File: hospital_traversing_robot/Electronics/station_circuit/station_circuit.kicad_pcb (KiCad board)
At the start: 2 copper layers, 17 parts, among them J1 Barrel_Jack_MountingPin, SW1 SW_Nidec_CAS-120A1, U1 Pico, U2 NRF24L01_Breakout, U3 LM338T

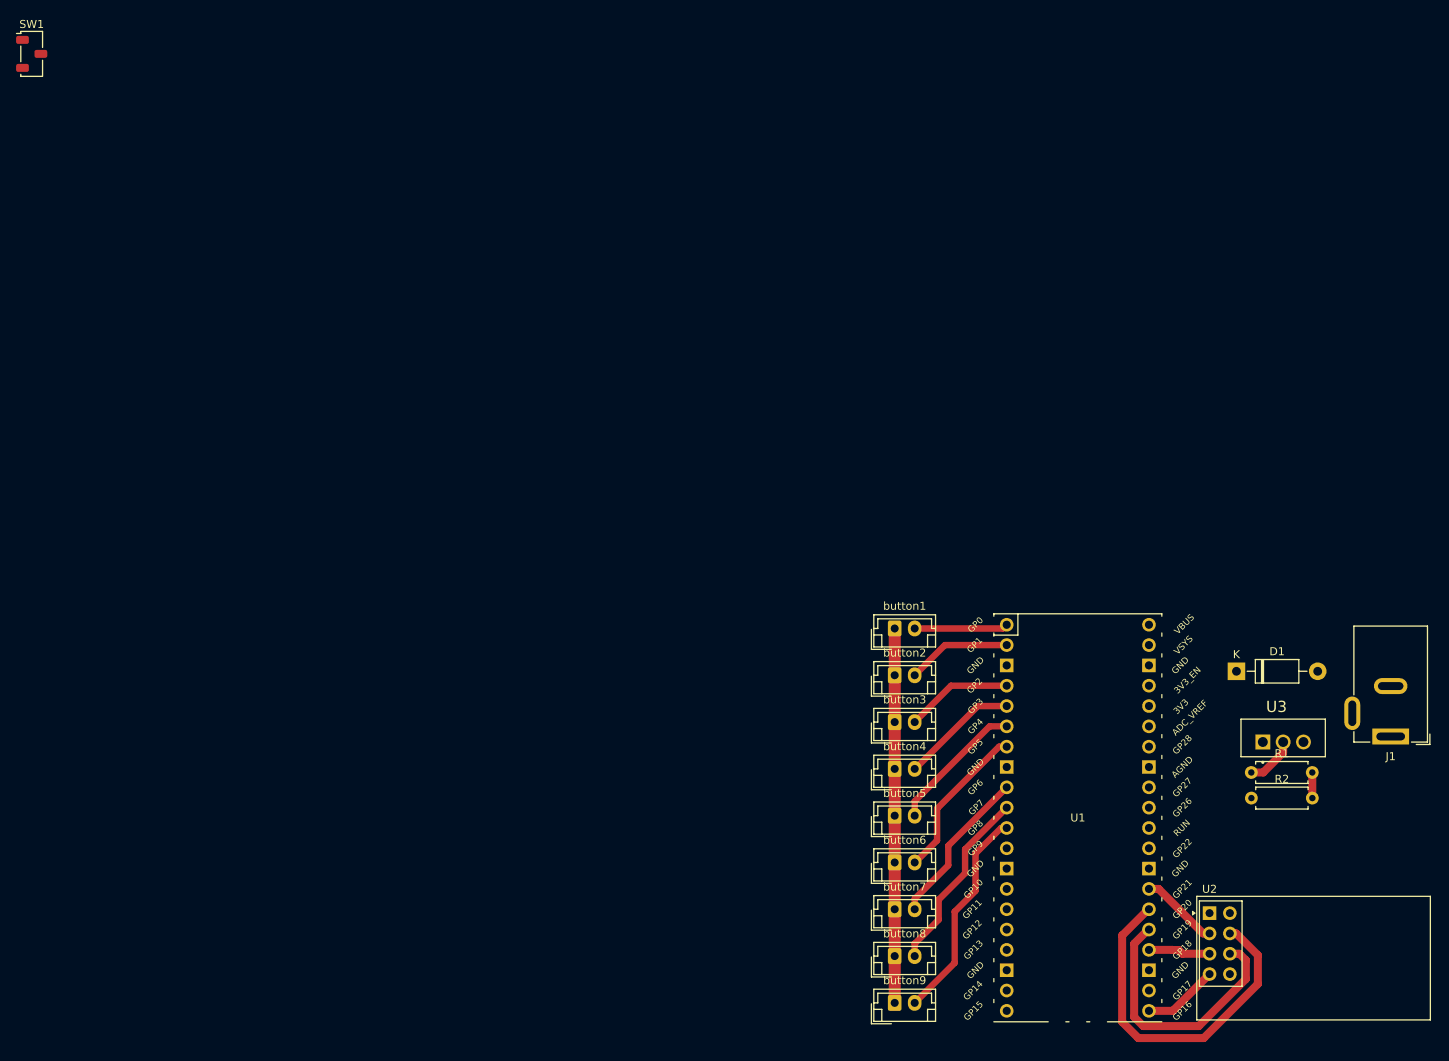
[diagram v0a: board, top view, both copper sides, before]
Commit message: finished station circuit PCB and started V2 product display stepper speaker circuit
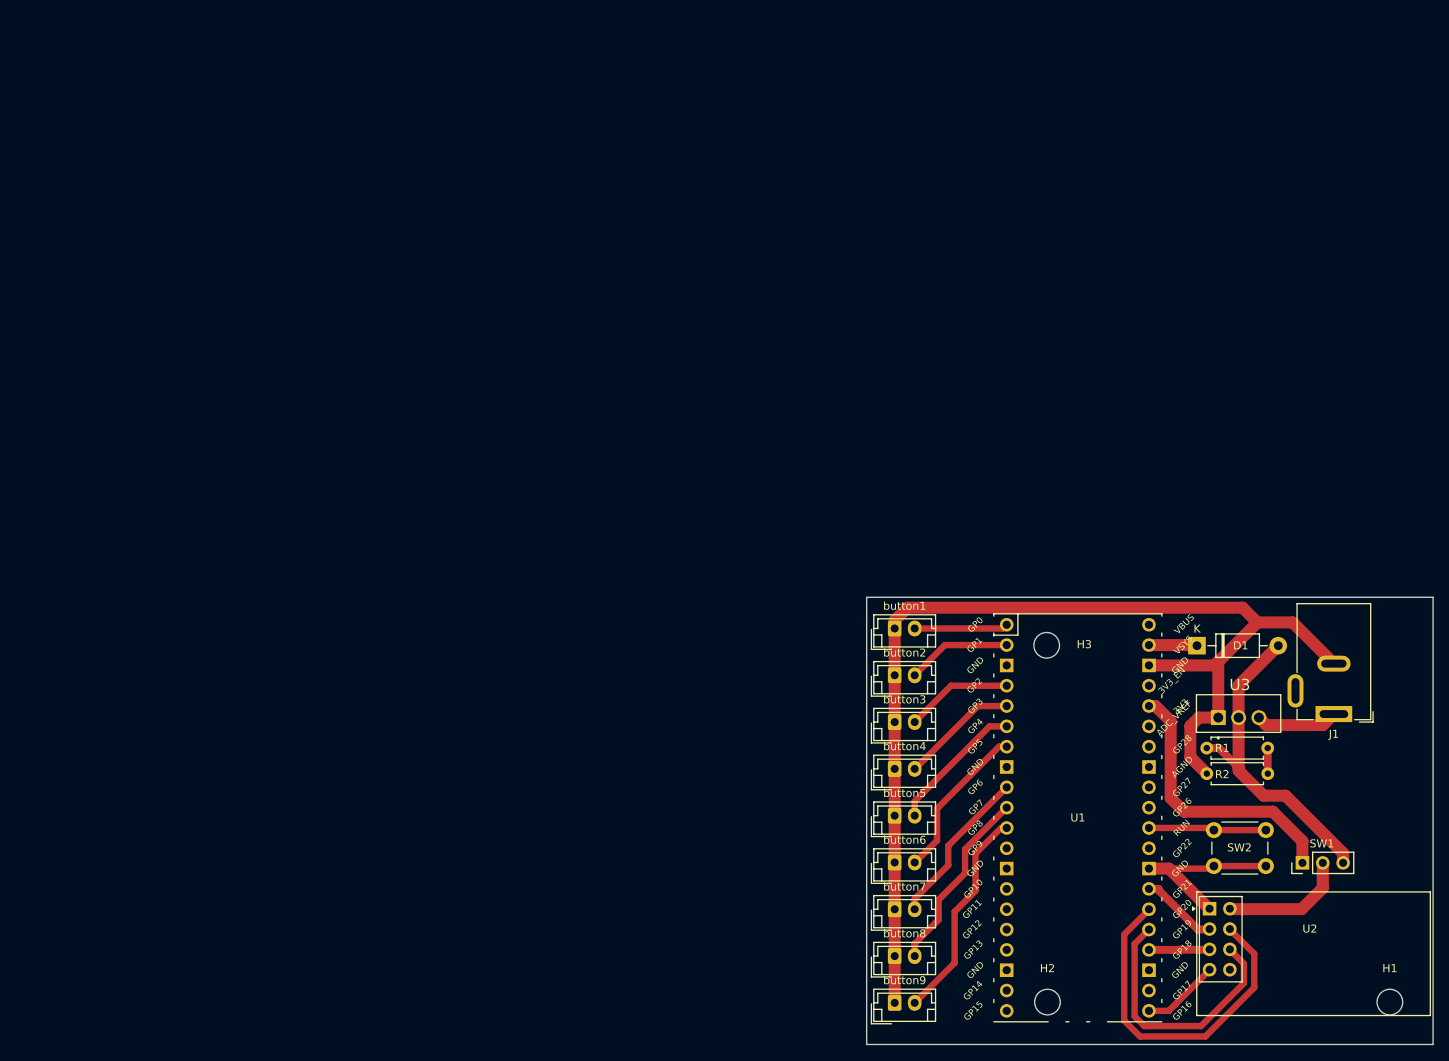
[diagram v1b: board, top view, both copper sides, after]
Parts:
- added H1: MountingHole, MountingHole:MountingHole_3.2mm_M3, F.Cu at (172.0, 121.5)
- added H2: MountingHole, MountingHole:MountingHole_3.2mm_M3, F.Cu at (129.2, 121.5)
- added H3: MountingHole, MountingHole:MountingHole_3.2mm_M3, F.Cu at (129.1, 76.9)
- added SW2: SW_Push, Button_Switch_THT:SW_PUSH_6mm, F.Cu at (150.0, 100.0)
- SW1: value SW_Nidec_CAS-120A1 -> switch; footprint Button_Switch_SMD:Nidec_Copal_CAS-120A -> Connector_PinHeader_2.54mm:PinHeader_1x03_P2.54mm_Vertical
- moved SW1 188.3 mm to (161.1, 104.1), turned to 90 degrees
- moved J1 7.63 mm to (165.0, 85.5)
- moved R1 6.35 mm to (149.1, 89.8)
- moved R2 6.35 mm to (149.1, 93.0)
- moved U3 6.35 mm to (153.1, 85.9)
- moved D1 5.88 mm to (147.9, 77.0)
- moved U2 0.55 mm to (149.5, 109.8)
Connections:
- D1 pad 1: unconnected-(D1-K-Pad1) -> Net-(D1-K)
- SW1 pad 1: unconnected-(SW1-C-Pad1) -> +3.3VA
- SW1 pad 2: unconnected-(SW1-B-Pad2) -> +3.3VP
- SW1 pad 3: unconnected-(SW1-A-Pad3) -> +3.3V
- U1 pad 28: unconnected-(U1-GND-Pad28) -> GNDA
- U1 pad 30: unconnected-(U1-RUN-Pad30) -> Net-(U1-RUN)
- U1 pad 36: unconnected-(U1-3V3-Pad36) -> +3.3VA
- U1 pad 39: unconnected-(U1-VSYS-Pad39) -> Net-(D1-K)
- U2 pad 1: GND -> GNDA
- U2 pad 2: +3.3V -> +3.3VP
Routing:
- net GND: track 46.8 -> 139.8 mm
- net +3.3V: track 6.33 -> 41.2 mm
- net +3.3VA: track 0.00 -> 34.5 mm
- net GNDA: track 0.00 -> 24.4 mm
- net +3.3VP: track 0.00 -> 15.9 mm
- net Net-(U1-RUN): track 0.00 -> 14.7 mm
- net +VDC: track 0.00 -> 10.3 mm
- net Net-(D1-K): track 0.00 -> 6.04 mm
- net CSN: track 44.3 -> 43.3 mm
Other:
- board outline added: 70.8 x 55.9 mm
